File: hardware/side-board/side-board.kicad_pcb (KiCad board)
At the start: 4 copper layers, 102.6 x 19.8 mm, 301 parts, among them IC101 TPS62933DRLR, IC102 NUP2105LT1G, IC201 STM32C092KCT6, IC202 TCAN332DR, IC203 TPS56A37RPAR, IC204 INA181A1IDBVR, IC301 STM32C092KCT6, IC302 TCAN332DR, IC303 TPS56A37RPAR, IC304 INA181A1IDBVR, IC401 STM32C092KCT6, IC402 TCAN332DR, IC403 TPS56A37RPAR, IC404 INA181A1IDBVR, J101 Inter-board Connector, J102 Inter-board Connector, J103 XT30 VBAT, J104 SWD PWR, J201 Servo Connector, J202 Servo Connector, J203 Servo Connector, J205 Conn_01x06, J301 Servo Connector, J302 Servo Connector, J303 Servo Connector, J305 Conn_01x06, J401 Servo Connector, J402 Servo Connector, J403 Servo Connector, J405 Conn_01x06, Y201 Crystal_GND24, Y301 Crystal_GND24, Y401 Crystal_GND24

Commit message: Compacted sideboard
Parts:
- J205, J305, J405: value Conn_01x06 -> Conn_01x04; footprint Connector_JST:JST_XH_B6B-XH-A_1x06_P2.50mm_Vertical -> Connector_JST:JST_XH_B4B-XH-A_1x04_P2.50mm_Vertical
- R305, R306, R307, R308, R312, R313, R405, R406, R407, R408, R412, R413: moved to B.Cu
- moved C311 98.2 mm to (226.6, 89.1)
- moved C411 98.2 mm to (226.8, 112.7)
- moved IC302 96.0 mm to (224.6, 83.4)
- moved IC402 96.0 mm to (224.8, 107.0)
- moved R320 93.4 mm to (226.5, 87.9)
- moved R420 93.4 mm to (226.7, 111.5)
- moved C308 90.5 mm to (230.7, 76.8)
- moved C408 90.5 mm to (230.9, 100.4)
- moved R306 90.5 mm to (224.1, 82.5)
- moved R406 90.5 mm to (224.3, 106.1)
- moved R308 90.5 mm to (224.1, 83.9)
- moved R408 90.5 mm to (224.3, 107.5)
- moved R313 90.5 mm to (224.1, 85.4)
- moved R413 90.5 mm to (224.3, 109.0)
- moved R325 90.3 mm to (231.2, 78.3)
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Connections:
- IC201 pad 28: /Leg_A/TOF_INT -> unconnected-(IC201-PB4-Pad28)
- IC201 pad 29: /Leg_A/TOF_SHUT -> unconnected-(IC201-PB5-Pad29)
- IC301 pad 28: /Leg_B/TOF_INT -> unconnected-(IC301-PB4-Pad28)
- IC301 pad 29: /Leg_B/TOF_SHUT -> unconnected-(IC301-PB5-Pad29)
- IC401 pad 28: /Leg_C/TOF_INT -> unconnected-(IC401-PB4-Pad28)
- IC401 pad 29: /Leg_C/TOF_SHUT -> unconnected-(IC401-PB5-Pad29)
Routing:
- net /Leg_B/PC6: track 0.00 -> 10.6 mm
- net /Leg_C/PC6: track 0.00 -> 10.6 mm
- net /Leg_B/6V0: track 15.0 -> 25.5 mm
- net /Leg_C/6V0: track 15.0 -> 25.5 mm
- net /~{ESTOP_N}: track 4.26 -> 12.8 mm
- net /Leg_C/CAN_TX: track 0.00 -> 7.06 mm
- net /Leg_B/CAN_TX: track 0.00 -> 7.06 mm
- net /Leg_B/OSC_OUT: track 6.04 -> 0.00 mm
- net /Leg_C/OSC_OUT: track 6.04 -> 0.00 mm
- net /Leg_C/TIM_PWM_TIBIA: track 0.00 -> 4.72 mm, vias 0 -> 1
- net /Leg_B/TIM_PWM_TIBIA: track 0.00 -> 4.72 mm, vias 0 -> 1
- net /Leg_C/TIM_PWM_FEMUR: track 0.00 -> 4.60 mm, vias 0 -> 1
- net /Leg_B/TIM_PWM_FEMUR: track 0.00 -> 4.60 mm, vias 0 -> 1
- net /Leg_C/TIM_PWM_COXA: track 0.00 -> 4.34 mm, vias 0 -> 1
- net /Leg_B/TIM_PWM_COXA: track 0.00 -> 4.34 mm, vias 0 -> 1
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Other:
- board size 102.6 x 19.8 mm -> 87.8 x 16.8 mm

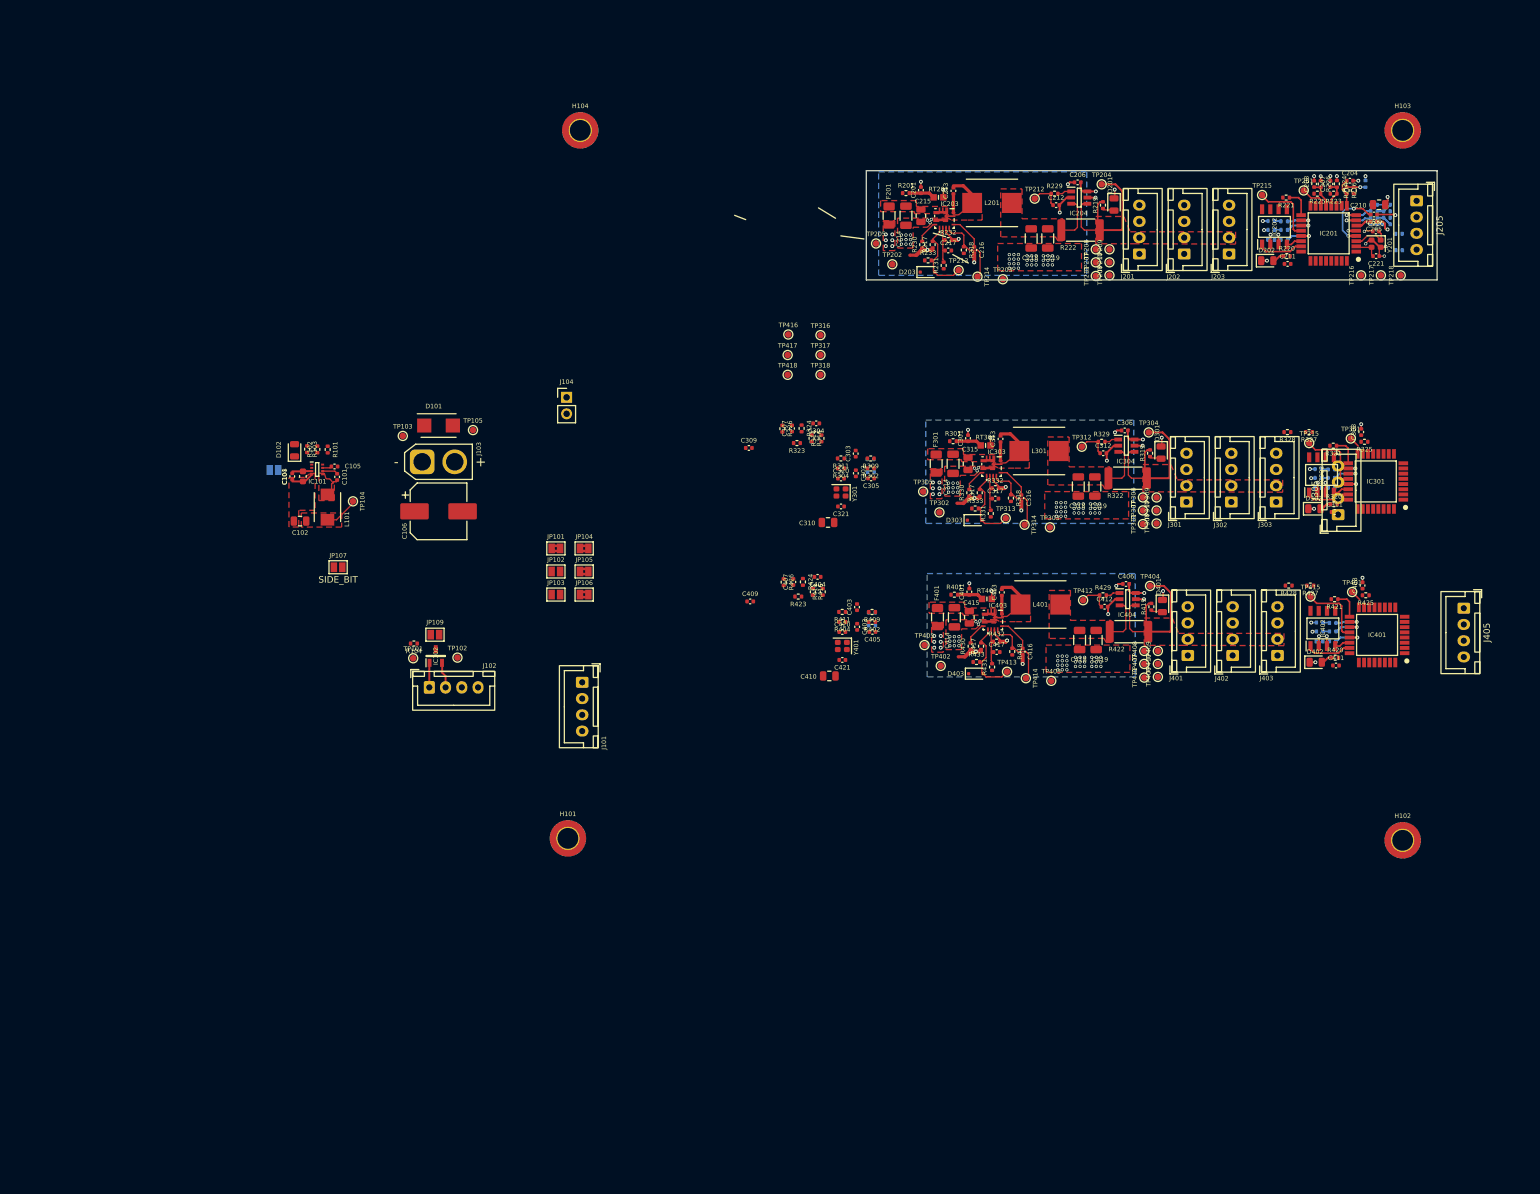
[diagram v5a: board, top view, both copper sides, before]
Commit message: Compacted sideboard further
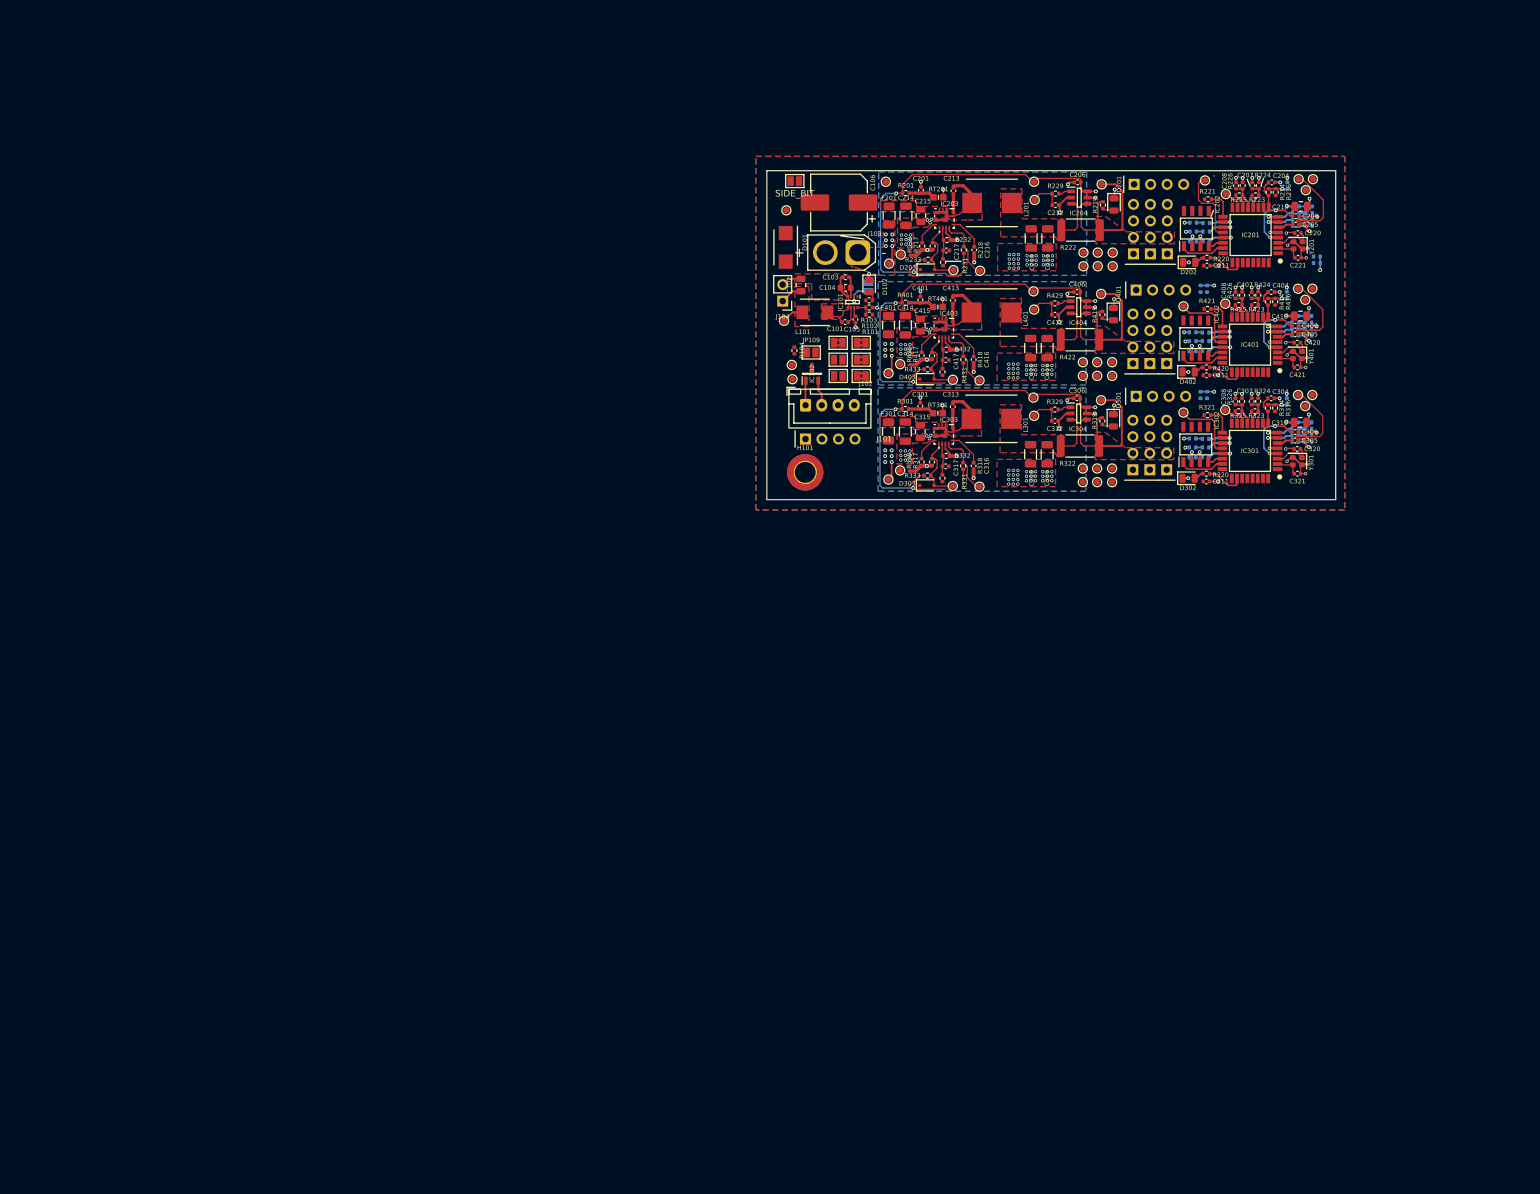
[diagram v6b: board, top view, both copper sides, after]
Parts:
- removed H102, H103, H104: M3, MountingHole:MountingHole_3.2mm_M3_DIN965_Pad_TopBottom
- C302, C303, C402, C403, R302, R304, R309, R311, R327, R328, R402, R404, R409, R411, R427, R428: moved to B.Cu
- J101, J201, J202, J203, J301, J302, J303, J401, J402, J403: footprint Connector_JST:JST_XH_B4B-XH-A_1x04_P2.50mm_Vertical -> vector:PinHeader_1x04_P2.54mm_Vertical_Tile
- J205, J305, J405: value Conn_01x04 -> ToF; footprint Connector_JST:JST_XH_B4B-XH-A_1x04_P2.50mm_Vertical -> vector:PinHeader_1x04_P2.54mm_Vertical_Tile
- moved JP108 95.7 mm to (154.9, 54.5), turned to -90 degrees
- moved C409 94.0 mm to (220.6, 60.5), turned to 180 degrees
- moved JP107 92.0 mm to (143.6, 38.2)
- moved D102 91.9 mm to (155.0, 54.3), turned to -90 degrees
- moved C410 91.2 mm to (221.4, 59.0)
- moved C103 90.5 mm to (151.4, 53.0), turned to 0 degrees
- moved R103 89.4 mm to (155.0, 56.5), turned to 180 degrees
- moved C104 88.4 mm to (151.4, 54.6), turned to 0 degrees
- moved R102 87.6 mm to (155.0, 57.6), turned to 0 degrees
- moved IC101 86.3 mm to (152.5, 56.8), turned to -90 degrees
- moved R415 86.0 mm to (219.3, 55.8)
- moved R101 85.8 mm to (155.0, 58.7), turned to 180 degrees
- moved C102 85.2 mm to (144.5, 54.2), turned to -90 degrees
- moved C309 84.1 mm to (220.6, 76.8), turned to 180 degrees
- moved R423 83.4 mm to (214.4, 57.3)
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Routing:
- net +3V3: track 31.4 -> 244.5 mm, vias 8 -> 27
- net GND: track 71.1 -> 125.3 mm, vias 172 -> 201
- net /Leg_C/NRST: track 0.00 -> 15.4 mm
- net /Leg_B/NRST: track 0.00 -> 15.4 mm
- net /Leg_A/NRST: track 2.49 -> 15.4 mm
- net /VBAT: track 3.01 -> 11.9 mm
- net /Leg_C/ADC_POT_FEMUR: track 0.00 -> 6.43 mm, vias 0 -> 1
- net /Leg_B/ADC_POT_FEMUR: track 0.00 -> 6.43 mm, vias 0 -> 1
- net /Leg_C/ADC_POT_COXA: track 0.00 -> 6.34 mm, vias 0 -> 1
- net /Leg_B/ADC_POT_COXA: track 0.00 -> 6.34 mm, vias 0 -> 1
- net /Leg_B/OSC_OUT: track 0.00 -> 5.92 mm
- net /Leg_C/OSC_OUT: track 0.00 -> 5.92 mm
- net /Leg_B/PA15: track 0.00 -> 5.63 mm
- net /Leg_C/PA15: track 0.00 -> 5.63 mm
- net /Leg_A/PA15: track 0.00 -> 5.63 mm
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- added copper zone on In2.Cu, net +3V3
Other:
- board size 87.8 x 16.8 mm -> 87.5 x 50.6 mm

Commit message: Completed sideboard PCB
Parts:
- JP109, TP208, TP209, TP210, TP211, TP308, TP309, TP310, TP311, TP408, TP409, TP410, TP411: moved to B.Cu
- moved JP107 84.8 mm to (226.5, 56.2), turned to -90 degrees
- moved JP101 78.9 mm to (226.4, 42.4), turned to 90 degrees
- moved JP102 78.7 mm to (226.4, 45.8), turned to 90 degrees
- moved JP103 76.9 mm to (226.4, 79.0), turned to -90 degrees
- moved JP104 75.6 mm to (226.2, 85.0), turned to -90 degrees
- moved JP106 73.2 mm to (226.5, 59.5), turned to 90 degrees
- moved JP105 72.8 mm to (226.5, 62.9), turned to -90 degrees
- moved TP207 36.5 mm to (224.5, 48.4)
- moved TP307 36.5 mm to (224.4, 81.6)
- moved TP407 36.5 mm to (224.4, 65.2)
- moved TP206 34.0 mm to (224.1, 45.8)
- moved TP306 34.0 mm to (224.0, 79.0)
- moved TP406 34.0 mm to (224.0, 62.7)
- moved TP208 24.2 mm to (214.9, 40.0), turned to 180 degrees
- moved TP408 24.2 mm to (214.8, 56.9), turned to 180 degrees
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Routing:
- net /VBAT: track 11.9 -> 220.4 mm, vias 18 -> 22
- net /~{ESTOP_N}: track 12.8 -> 170.1 mm, vias 0 -> 11
- net /CAN_H: track 3.80 -> 135.7 mm, vias 0 -> 7
- net /CAN_L: track 4.08 -> 134.4 mm, vias 0 -> 7
- net /Leg_A/NTC_SENSE: track 3.69 -> 72.9 mm, vias 0 -> 2
- net /Leg_C/NTC_SENSE: track 3.69 -> 72.9 mm, vias 0 -> 2
- net /Leg_B/NTC_SENSE: track 3.69 -> 72.9 mm, vias 0 -> 2
- net /Leg_A/MCU_BUCK_EN: track 4.89 -> 66.6 mm, vias 0 -> 2
- net /SIDE_BIT: track 0.00 -> 60.2 mm, vias 0 -> 6
- net /Leg_C/6V0_BUCK: track 7.08 -> 64.0 mm, vias 0 -> 4
- net /Leg_A/6V0_BUCK: track 7.08 -> 64.0 mm, vias 0 -> 4
- net /Leg_B/6V0_BUCK: track 7.08 -> 64.0 mm, vias 0 -> 4
- net /Leg_C/MCU_BUCK_EN: track 3.50 -> 60.0 mm, vias 0 -> 2
- net /Leg_B/MCU_BUCK_EN: track 3.50 -> 59.9 mm, vias 0 -> 2
- net /Leg_C/BUCK_PG: track 9.49 -> 58.7 mm, vias 0 -> 3
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- added copper zone on In2.Cu, net /VBAT
